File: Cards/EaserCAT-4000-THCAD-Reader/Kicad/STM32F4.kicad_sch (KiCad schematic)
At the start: 40 parts, among them J1 Conn_01x02_Pin, J10 Conn_01x06_Pin, J11 Conn_01x06_Pin, J12 Conn_01x06_Pin, J13 Stepper 1, J14 Stepper 2, J2 Serial usart1, J3 STLINK, SW1 SW_Push, U3 AMS1117-3.3, U4 STM32F407VGT6, Y2 8 MHz

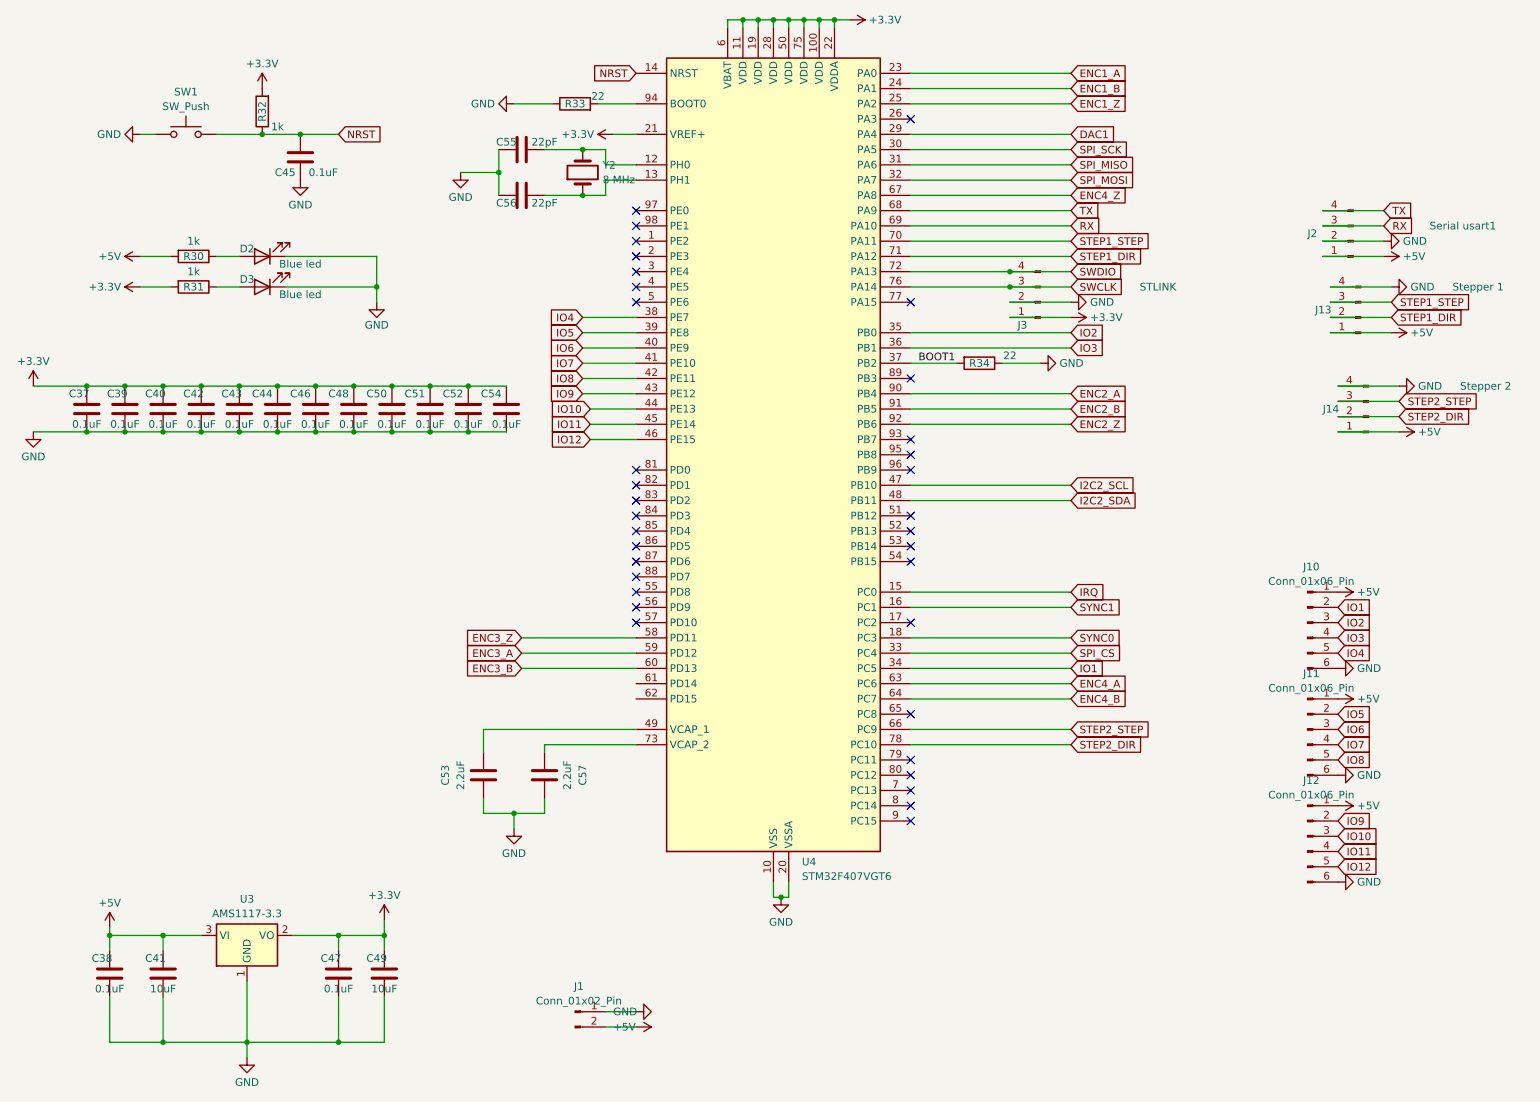
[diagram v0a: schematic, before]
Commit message: Moving all to Kicad8. Housekeeping symbols,libraries,3d-models
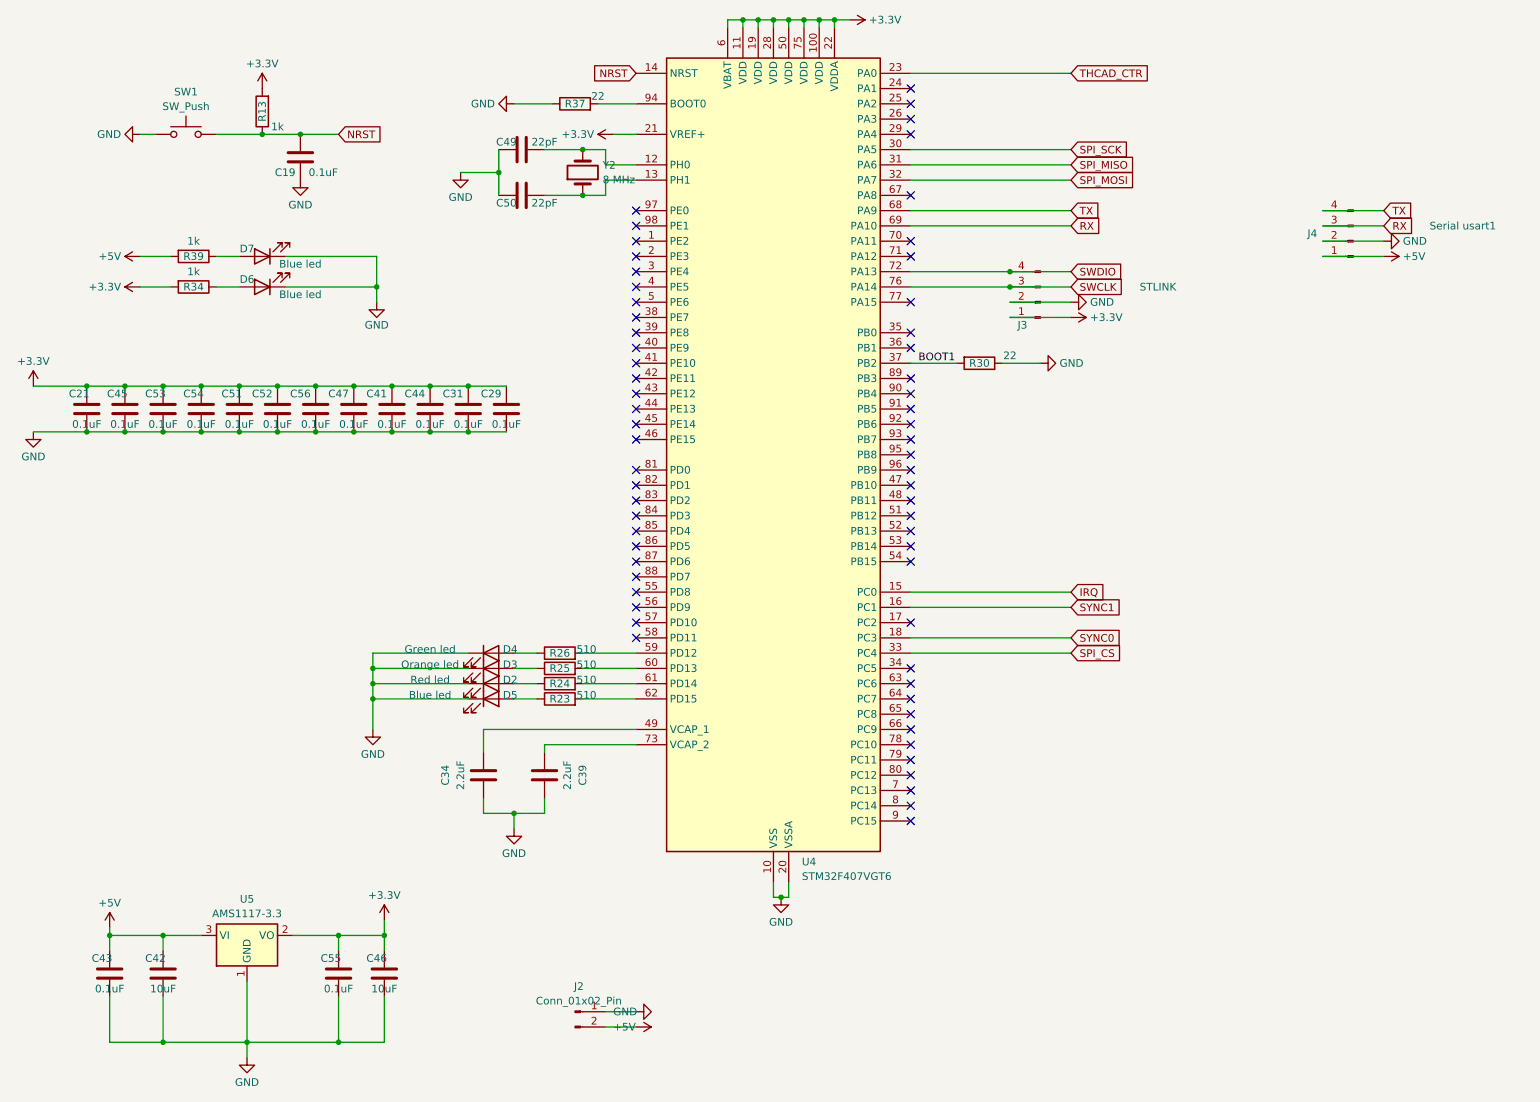
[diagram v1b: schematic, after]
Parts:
- removed J10, J11, J12: Conn_01x06_Pin, Connector_JST:JST_XH_B6B-XH-A_1x06_P2.50mm_Vertical, symbol Connector:Conn_01x06_Pin
- removed J13: Stepper 1, Connector_JST:JST_XH_B4B-XH-A_1x04_P2.50mm_Vertical, symbol Connector:Conn_01x04_Pin
- removed J14: Stepper 2, Connector_JST:JST_XH_B4B-XH-A_1x04_P2.50mm_Vertical, symbol Connector:Conn_01x04_Pin
- added D2: Red led, LED_SMD:LED_0805_2012Metric, symbol Device:LED
- added D3: Orange led, LED_SMD:LED_0805_2012Metric, symbol Device:LED
- added D4: Green led, LED_SMD:LED_0805_2012Metric, symbol Device:LED
- added D5: Blue led, LED_SMD:LED_0805_2012Metric, symbol Device:LED
- added R23, R24, R25, R26: 510, Resistor_SMD:R_0805_2012Metric, symbol Device:R
- Y2: footprint Crystal:Crystal_HC49-U_Vertical -> Crystal:Crystal_HC49-4H_Vertical
- renumbered C45 to C19, C37 to C21, C54 to C29, C52 to C31, C53 to C34, C57 to C39, C50 to C41, C41 to C42, C38 to C43, C51 to C44, C39 to C45, C49 to C46, C48 to C47, C55 to C49, C56 to C50, C43 to C51, C44 to C52, C40 to C53, C42 to C54, C47 to C55, C46 to C56, D3 to D6, D2 to D7, J1 to J2, J2 to J4, R32 to R13, R34 to R30, R31 to R34, R33 to R37, R30 to R39, U3 to U5
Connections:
- net GND: now also D2.1 (K), D3.1 (K), D4.1 (K), D5.1 (K)
- net at U4.61 (PD14): now also R24.2
- net at U4.62 (PD15): now also R23.2
- net DAC1: no longer names the net of U4.29 (PA4)
- net ENC1_A renamed THCAD_CTR
- net ENC1_B: no longer names the net of U4.24 (PA1)
- net ENC1_Z: no longer names the net of U4.25 (PA2)
- net ENC2_A: no longer names the net of U4.90 (PB4)
- net ENC2_B: no longer names the net of U4.91 (PB5)
- net ENC2_Z: no longer names the net of U4.92 (PB6)
- net ENC3_A: no longer names the net of U4.59 (PD12)
- net ENC3_A: now also R26.2
- net ENC3_B: no longer names the net of U4.60 (PD13)
- net ENC3_B: now also R25.2
- net ENC3_Z: no longer names the net of U4.58 (PD11)
- net ENC4_A: no longer names the net of U4.63 (PC6)
- net ENC4_B: no longer names the net of U4.64 (PC7)
- net ENC4_Z: no longer names the net of U4.67 (PA8)
- net I2C2_SCL: no longer names the net of U4.47 (PB10)
- net I2C2_SDA: no longer names the net of U4.48 (PB11)
- net IO1: no longer names the net of U4.34 (PC5)
- net IO10: no longer names the net of U4.44 (PE13)
- net IO11: no longer names the net of U4.45 (PE14)
- net IO12: no longer names the net of U4.46 (PE15)
- net IO2: no longer names the net of U4.35 (PB0)
- net IO3: no longer names the net of U4.36 (PB1)
- net IO4: no longer names the net of U4.38 (PE7)
- net IO5: no longer names the net of U4.39 (PE8)
- net IO6: no longer names the net of U4.40 (PE9)
- net IO7: no longer names the net of U4.41 (PE10)
- net IO8: no longer names the net of U4.42 (PE11)
- net IO9: no longer names the net of U4.43 (PE12)
- net STEP1_DIR: no longer names the net of U4.71 (PA12)
- net STEP1_STEP: no longer names the net of U4.70 (PA11)
- net STEP2_DIR: no longer names the net of U4.78 (PC10)
- net STEP2_STEP: no longer names the net of U4.66 (PC9)
- new net: D3.2 (A), R25.1
- new net: D2.2 (A), R24.1
- new net: D5.2 (A), R23.1
- new net: D4.2 (A), R26.1
- no-connect marks 35 -> 63
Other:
- title: (none) -> THCAD reader
